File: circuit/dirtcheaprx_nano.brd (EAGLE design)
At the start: 19.6 x 24.4 mm, 23 parts, among them IC1 MCP1703T-3302E/CB

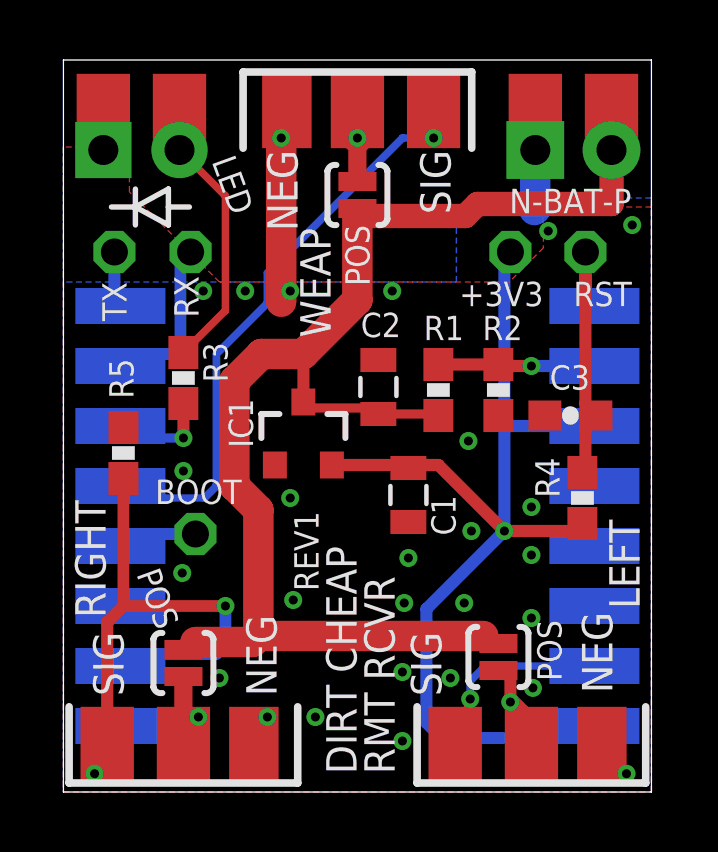
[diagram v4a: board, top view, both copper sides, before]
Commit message: resistor on GPIO0, flipped weap servo connector
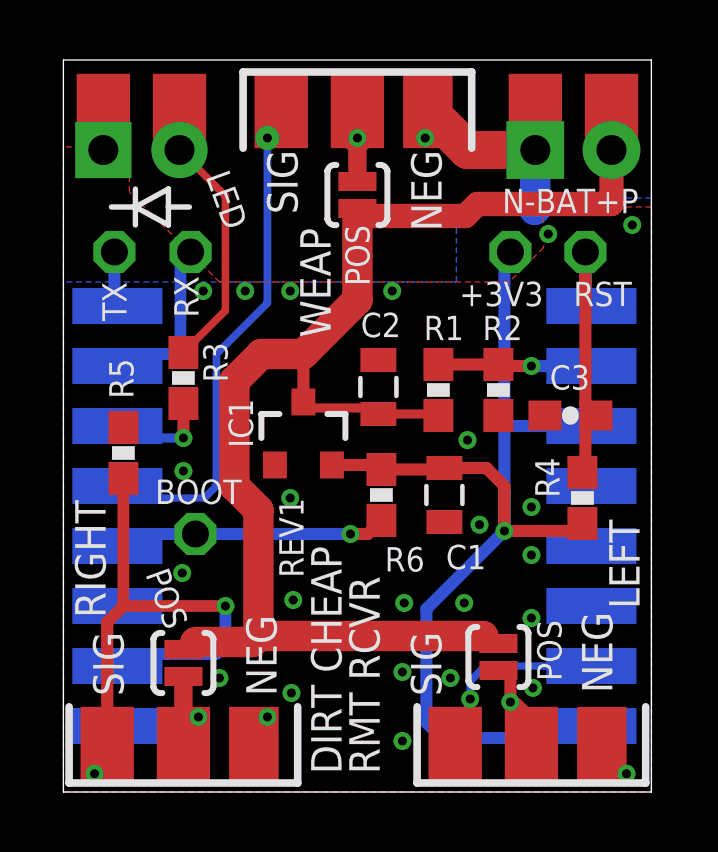
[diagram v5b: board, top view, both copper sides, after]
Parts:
- added R6: 5K6Ω, dirtcheaprx_nano:0603-RES
- SERVO1: value SERVO-SMD-EDGE-1 -> SERVO-SMD-EDGE-1F; device dirtcheaprx_nano:SERVO-EDGE -> dirtcheaprx_nano:SERVO-EDGE-F
- moved C1 1.20 mm to (12.7, 9.90)
- moved U1 0.10 mm to (9.70, 10.6)
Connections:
- net 3.3V: now also R6.1
- net N$11: now also R6.2
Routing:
- net N$11: track 2.67 -> 9.13 mm, vias 0 -> 1
- net SIG-WEAP: track 19.9 -> 17.2 mm
- net GND: track 9.71 -> 8.23 mm, vias 27 -> 26
- net 3.3V: track 35.8 -> 36.6 mm
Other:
- board text added: "N-BAT+P"
- board text removed: "N-BAT-P"

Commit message: gerbers ordered
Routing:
- net N$4: track 3.13 -> 4.28 mm
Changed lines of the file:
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@@
 <wire x1="14.9" y1="3" x2="14.9" y2="4.05" width="0.4064" layer="1"/>
 <wire x1="14.9" y1="4.05" x2="14.5" y2="4.05" width="0.4064" layer="1"/>
+<wire x1="14.6" y1="3.9" x2="14.6" y2="3.1" width="0.254" layer="1"/>
+<wire x1="14.6" y1="3.1" x2="14.7" y2="3" width="0.254" layer="1"/>
+<wire x1="14.7" y1="3" x2="14.9" y2="3" width="0.254" layer="1"/>
 </signal>
 <signal name="SIG-RIGHT">
